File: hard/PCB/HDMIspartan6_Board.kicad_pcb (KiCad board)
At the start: 4 copper layers, 60 x 85.1 mm, 151 parts, among them IC1 W9812G6KH, J1 CONN_02X20, P1 CONN_01X03, U1 XC6SLX9-2TQG144C, U2 TPS62133RGTR, U3 ZLDO1117G33TA, U4 ZLDO1117G12TA, U5 MAX5864

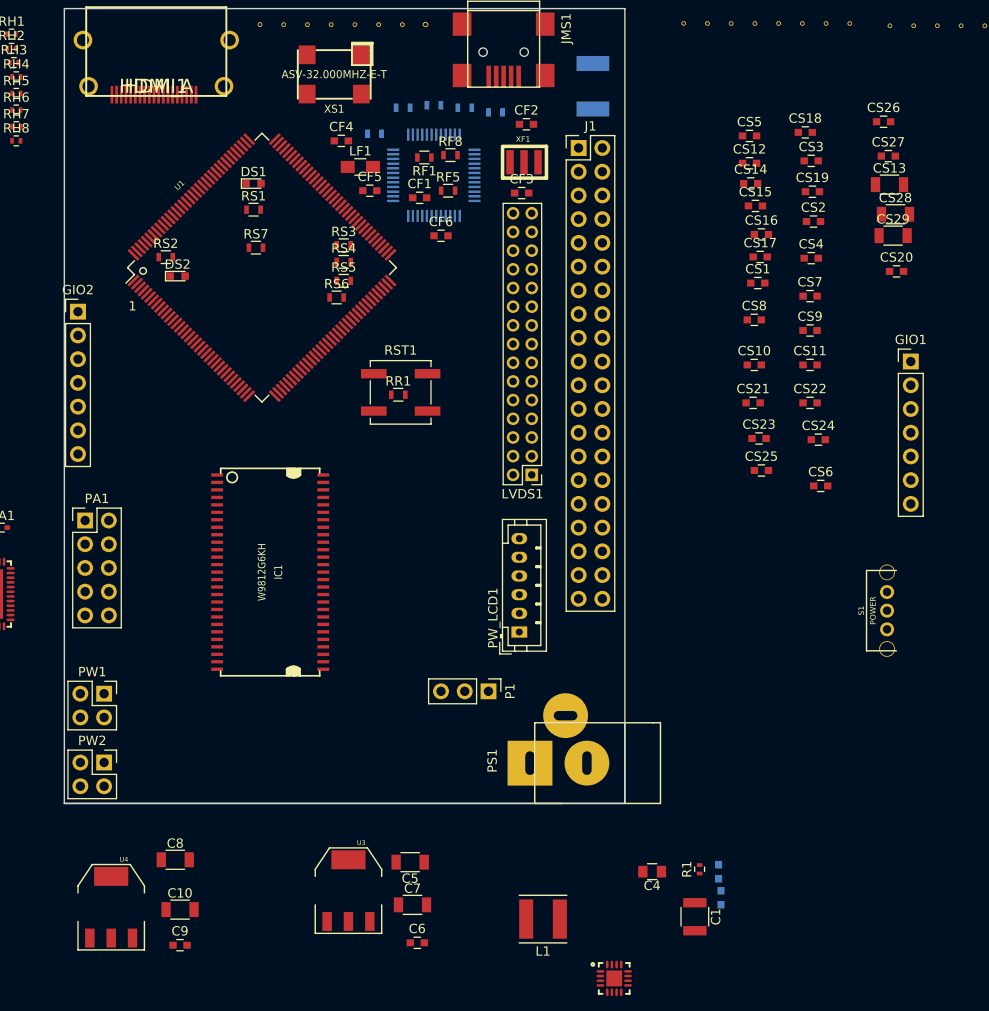
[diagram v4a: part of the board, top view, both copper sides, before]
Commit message: update 3d models
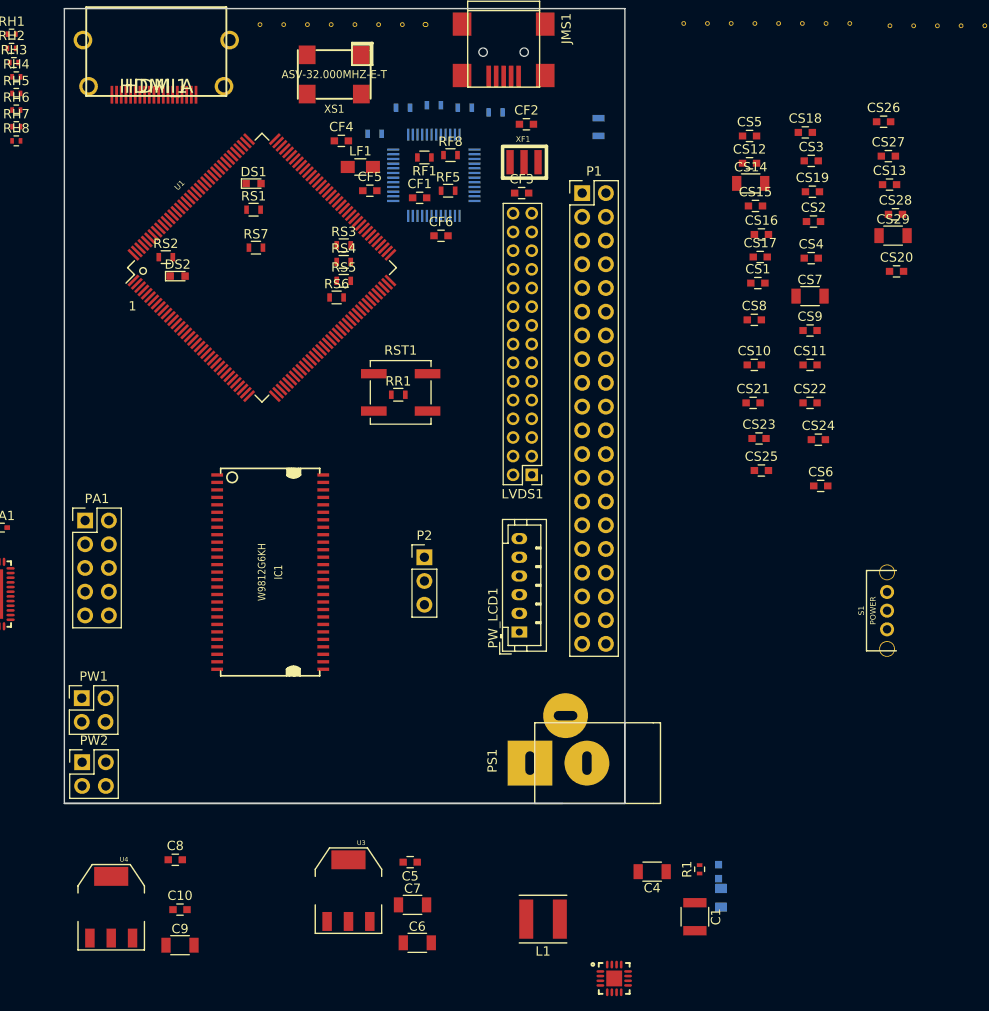
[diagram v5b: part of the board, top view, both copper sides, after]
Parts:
- removed GIO1, GIO2: CONN_01X07, Pin_Headers:Pin_Header_Straight_1x07_Pitch2.54mm
- removed J1: CONN_02X20, Pin_Headers:Pin_Header_Straight_2x20_Pitch2.54mm
- added P2: CONN_01X03, Pin_Headers:Pin_Header_Straight_1x03_Pitch2.54mm, F.Cu at (95.2, 96.3)
- C10: value 33uF -> 3.3nF; footprint Capacitors_SMD:C_1206 -> Capacitors_SMD:C_0603
- C3: value 3.3nF -> 22uF; footprint Capacitors_SMD:C_0603 -> Capacitors_SMD:C_0805
- C4: value 22uF -> 33uF; footprint Capacitors_SMD:C_0805 -> Capacitors_SMD:C_1206
- C5, C8: value 33uF -> 100n; footprint Capacitors_SMD:C_1206 -> Capacitors_SMD:C_0603
- C6, C9: value 100n -> 33uF; footprint Capacitors_SMD:C_0603 -> Capacitors_SMD:C_1206
- CF1: value 47pF -> 10nF
- CF2: value 47pF -> 10uF
- CF3: value 10nF -> 100nF
- CF4: value 10uF -> 33nF
- CF5: value 33nF -> 47pF
- CF6: value 100nF -> 47pF
- CS11, CS26, CS27: value 1uF -> 0.1uF
- CS13, CS28: value 4.7uF -> 1uF; footprint Capacitors_SMD:C_1206 -> Capacitors_SMD:C_0603
- CS14, CS7: value 0.1uF -> 4.7uF; footprint Capacitors_SMD:C_0603 -> Capacitors_SMD:C_1206
- CS6: value 0.1uF -> 1uF
- F1: footprint Resistors_SMD:R_1812 -> Resistors_SMD:R_0805
- P1: value CONN_01X03 -> CONN_02X20; footprint Socket_Strips:Socket_Strip_Straight_1x03_Pitch2.54mm -> Pin_Headers:Pin_Header_Straight_2x20_Pitch2.54mm
- PW1, PW2: footprint Socket_Strips:Socket_Strip_Straight_2x02_Pitch2.54mm -> Pin_Headers:Pin_Header_Straight_2x02_Pitch2.54mm
- RF1: value 27R -> 470R
- RF3: value 1K5 -> 27R
- RF4: value 10K -> 15K
- RF5: value 470R -> 1K5
- RF7: value 10k -> 10K
- RF8: value 15K -> 10k
- RS1, RS2: value 1k -> 68
- RS5: value 68 -> 4.7k
- RS6: value 68 -> 1k
- RS7: value 4.7k -> 1k
- moved P1 54.3 mm to (112.1, 57.3), turned to 0 degrees
- moved F1 4.41 mm to (113.9, 50.2)
- moved PW1 2.44 mm to (58.6, 111.4)
- moved PW2 2.35 mm to (58.6, 118.2)
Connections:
- C10 pad 1: +1V2 -> Net-(C10-Pad1)
- C3 pad 1: Net-(C3-Pad1) -> VDD5V
- C4 pad 1: VDD5V -> +5V
- C5 pad 1: +5V -> +3V3
- C8 pad 1: +3V3 -> +1V2
- CA1 pad 1: /ADC_DAC/REFP -> /ADC_DAC/COM
- CA2 pad 1: /ADC_DAC/COM -> /ADC_DAC/REFN
- CA3 pad 1: /ADC_DAC/REFN -> /ADC_DAC/REFP
- CF1 pad 1: GND -> /Power/USBVCC
- CF1 pad 2: Net-(CF1-Pad2) -> GND
- CF2 pad 1: GND -> /serial_interface/+5VA
- CF2 pad 2: Net-(CF2-Pad2) -> GND
- CF3 pad 1: /Power/USBVCC -> Net-(CF3-Pad1)
- CF4 pad 1: /serial_interface/+5VA -> Net-(CF4-Pad1)
- CF5 pad 1: Net-(CF5-Pad1) -> GND
- CF5 pad 2: GND -> Net-(CF5-Pad2)
- CF6 pad 1: Net-(CF6-Pad1) -> GND
- CF6 pad 2: GND -> Net-(CF6-Pad2)
- CS10 pad 1: +3V3 -> +1V2
- CS11 pad 1: +3V3 -> +1V2
- CS12 pad 1: +3V3 -> +1V2
- CS13 pad 1: +3V3 -> +1V2
- CS14 pad 1: +3V3 -> +1V2
- CS17 pad 1: +1V2 -> +3V3
- CS19 pad 1: +1V2 -> +3V3
- CS21 pad 1: +1V2 -> +3V3
- CS23 pad 1: +1V2 -> +3V3
- CS25 pad 1: +1V2 -> +3V3
- CS27 pad 1: +1V2 -> +3V3
- CS29 pad 1: +1V2 -> +3V3
- CS8 pad 1: +3V3 -> +1V2
- CS9 pad 1: +3V3 -> +1V2
- FT1 pad 43: Net-(CF1-Pad2) -> Net-(CF5-Pad2)
- FT1 pad 44: Net-(CF2-Pad2) -> Net-(CF6-Pad2)
- FT1 pad 46: Net-(CF6-Pad1) -> Net-(CF3-Pad1)
- FT1 pad 6: Net-(CF5-Pad1) -> Net-(CF4-Pad1)
- P1 pad 1: VDD5V -> +3V3
- P1 pad 2: +5V -> VDD5V
- P1 pad 3: /Power/USBVCC -> /spartan6/SDA
- RF1 pad 1: Net-(JMS1-Pad2) -> Net-(CF3-Pad1)
- RF1 pad 2: Net-(FT1-Pad8) -> /serial_interface/+5VA
- RF2 pad 1: Net-(JMS1-Pad3) -> Net-(JMS1-Pad2)
- RF2 pad 2: Net-(FT1-Pad7) -> Net-(FT1-Pad8)
- RF3 pad 1: Net-(FT1-Pad7) -> Net-(JMS1-Pad3)
- RF3 pad 2: Net-(FT1-Pad5) -> Net-(FT1-Pad7)
- RF4 pad 1: /serial_interface/+5VA -> +3V3
- RF4 pad 2: Net-(FT1-Pad2) -> /spartan6/F_RXD
- RF5 pad 1: Net-(CF6-Pad1) -> Net-(FT1-Pad7)
- RF5 pad 2: /serial_interface/+5VA -> Net-(FT1-Pad5)
- RF7 pad 1: Net-(FT1-Pad26) -> /serial_interface/+5VA
- RF7 pad 2: +3V3 -> Net-(FT1-Pad2)
- RF8 pad 1: +3V3 -> Net-(FT1-Pad26)
- RF8 pad 2: /spartan6/F_RXD -> +3V3
- RS1 pad 1: GND -> /spartan6/F_TCK
- RS1 pad 2: Net-(DS1-Pad2) -> Net-(RS1-Pad2)
- RS2 pad 1: GND -> /spartan6/F_TDI
- RS2 pad 2: Net-(DS2-Pad2) -> Net-(RS2-Pad2)
- RS3 pad 1: /spartan6/F_TCK -> /spartan6/F_TDO
- RS4 pad 1: /spartan6/F_TDI -> /spartan6/F_TMS
- RS5 pad 1: /spartan6/F_TDO -> +3V3
- RS6 pad 1: /spartan6/F_TMS -> GND
- RS6 pad 2: Net-(RS6-Pad2) -> Net-(DS1-Pad2)
- RS7 pad 1: +3V3 -> GND
- RS7 pad 2: Net-(RS7-Pad2) -> Net-(DS2-Pad2)
- U1 pad 106: Net-(RS5-Pad2) -> Net-(RS3-Pad2)
- U1 pad 107: Net-(RS6-Pad2) -> Net-(RS4-Pad2)
- U1 pad 109: Net-(RS3-Pad2) -> Net-(RS1-Pad2)
- U1 pad 110: Net-(RS4-Pad2) -> Net-(RS2-Pad2)
- U1 pad 38: Net-(RS7-Pad2) -> Net-(RS5-Pad2)
- U2 pad 9: Net-(C3-Pad1) -> Net-(C10-Pad1)
- XF1 pad 1: Net-(CF1-Pad2) -> Net-(CF5-Pad2)
- XF1 pad 3: Net-(CF2-Pad2) -> Net-(CF6-Pad2)

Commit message: reorganización
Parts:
- LF1: footprint Resistors_SMD:R_0805_HandSoldering -> Resistors_SMD:R_0805
- moved PS1 93.5 mm to (109.7, 24.9)
- moved JMS1 75.6 mm to (38.5, 79.5)
- moved PW_LCD1 27.7 mm to (104.7, 76.6)
- moved LVDS1 25.4 mm to (105.8, 112.9)
- moved P1 21.1 mm to (123.3, 75.2)
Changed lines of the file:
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@@
-(kicad_pcb (version 4) (host pcbnew 4.0.6-e0-6349~53~ubuntu16.04.1)
+(kicad_pcb (version 4) (host pcbnew 4.0.5)
   (general
     (links 443)
@@
   )
   (module Connectors_JST:JST_PH_B6B-PH-K_06x2.00mm_Straight (layer F.Cu)
-    (at 105.4 104.286 90)
+    (at 104.71166 76.55682 90)
     (descr "JST PH series connector, B6B-PH-K, top entry type, through hole, Datasheet: http://www.jst-mfg.com/product/pdf/eng/ePH.pdf")
     (tags "connector jst ph")
@@
   )
   (module Pin_Headers:Pin_Header_Straight_2x15_Pitch2.00mm (layer F.Cu)
-    (at 106.7335 87.4585 180)
+    (at 105.82926 112.87882 180)
     (descr "Through hole straight pin header, 2x15, 2.00mm pitch, double rows")
     (tags "Through hole pin header THT 2x15 2.00mm double row")
@@
     (pad "" thru_hole circle (at 4.1 0 90) (size 1.7 1.7) (drill 1.5) (layers *.Cu *.Mask F.SilkS))
     (pad "" thru_hole circle (at -4.1 0 90) (size 1.7 1.7) (drill 1.5) (layers *.Cu *.Mask F.SilkS))
-    (model /media/raparram/E4AA707DAA704DD4/Users/Ryu/Documents/GitHub/hdmi-fpga/hard/PCB/packages3d/slide-sw-spdt-right-angle.wrl
+    (model ${KIPRJMOD}/packages3d/slide-sw-spdt-right-angle.wrl
       (at (xyz 0 0 0))
       (scale (xyz 1 1 1))
@@
   )
   (module Project:USB_Mini-B (layer F.Cu)
-    (at 103.7236 41.3575 270)
+    (at 38.45576 79.45242 270)
     (descr "USB Mini-B 5-pin SMD connector")
     (tags "USB USB_B USB_Mini connector")
@@
     (pad "" np_thru_hole circle (at 0.8509 2.19964 270) (size 0.89916 0.89916) (drill 0.89916) (layers *.Cu *.Mask F.SilkS))
     (model ${KIPRJMOD}/packages3d/usb.wrl
-      (at (xyz 0 0 0))
-      (scale (xyz 1 1 1))
-      (rotate (xyz 0 0 0))
+      (at (xyz 0.15 0 0))
+      (scale (xyz 0.42 0.42 0.42))
+      (rotate (xyz -90 0 90))
     )
   )
@@
   )
   (module Project:JACK_ALIM (layer F.Cu)
-    (at 112.639 118.3195 180)
+    (at 109.72816 24.89322 180)
     (descr "module 1 pin (ou trou mecanique de percage)")
     (tags "CONN JACK")
@@
     )
   )
-  (module Resistors_SMD:R_0805_HandSoldering (layer F.Cu)
-    (at 88.382 54.502)
-    (descr "Resistor SMD 0805, hand soldering")
-    (tags "resistor 0805")
-    (attr smd)
-    (fp_text reference LF1 (at 0 -1.7) (layer F.SilkS)
-      (effects (font (size 1 1) (thickness 0.15)))
-    )
-    (fp_text value HZ0805D152R-10 (at 0 1.75) (layer F.Fab)
-      (effects (font (size 1 1) (thickness 0.15)))
-    )
-    (fp_text user %R (at 0 0) (layer F.Fab)
-      (effects (font (size 0.5 0.5) (thickness 0.075)))
-    )
-    (fp_line (start -1 0.62) (end -1 -0.62) (layer F.Fab) (width 0.1))
-    (fp_line (start 1 0.62) (end -1 0.62) (layer F.Fab) (width 0.1))
-    (fp_line (start 1 -0.62) (end 1 0.62) (layer F.Fab) (width 0.1))
-    (fp_line (start -1 -0.62) (end 1 -0.62) (layer F.Fab) (width 0.1))
-    (fp_line (start 0.6 0.88) (end -0.6 0.88) (layer F.SilkS) (width 0.12))
-    (fp_line (start -0.6 -0.88) (end 0.6 -0.88) (layer F.SilkS) (width 0.12))
-    (fp_line (start -2.35 -0.9) (end 2.35 -0.9) (layer F.CrtYd) (width 0.05))
-    (fp_line (start -2.35 -0.9) (end -2.35 0.9) (layer F.CrtYd) (width 0.05))
-    (fp_line (start 2.35 0.9) (end 2.35 -0.9) (layer F.CrtYd) (width 0.05))
-    (fp_line (start 2.35 0.9) (end -2.35 0.9) (layer F.CrtYd) (width 0.05))
-    (pad 1 smd rect (at -1.35 0) (size 1.5 1.3) (layers F.Cu F.Paste F.Mask)
-      (net 51 /Power/USBVCC))
-    (pad 2 smd rect (at 1.35 0) (size 1.5 1.3) (layers F.Cu F.Paste F.Mask)
-      (net 80 /serial_interface/+5VA))
-    (model ${KISYS3DMOD}/Resistors_SMD.3dshapes/R_0805.wrl
-      (at (xyz 0 0 0))
-      (scale (xyz 1 1 1))
-      (rotate (xyz 0 0 0))
-    )
-  )
   (module Resistors_SMD:R_0402 (layer F.Cu)
     (at 51.044 40.278)
@@
     (model ${KIPRJMOD}/packages3d/Crystal_SMD_5032-4pin_5.0x3.2mm.wrl
       (at (xyz 0 0 0))
-      (scale (xyz 1 1 1))
+      (scale (xyz 1.55 1.55 1.55))
       (rotate (xyz 0 0 0))
     )
@@
   )
   (module Pin_Headers:Pin_Header_Straight_2x20_Pitch2.54mm (layer F.Cu)
-    (at 112.131 57.296)
+    (at 123.34256 75.18522)
     (descr "Through hole straight pin header, 2x20, 2.54mm pitch, double rows")
     (tags "Through hole pin header THT 2x20 2.54mm double row")
@@
     )
   )
+  (module Resistors_SMD:R_0805 (layer F.Cu)
+    (at 88.382 54.502)
+    (descr "Resistor SMD 0805, reflow soldering, Vishay (see dcrcw.pdf)")
+    (tags "resistor 0805")
+    (attr smd)
+    (fp_text reference LF1 (at 0 -1.65) (layer F.SilkS)
+      (effects (font (size 1 1) (thickness 0.15)))
+    )
+    (fp_text value HZ0805D152R-10 (at 0 1.75) (layer F.Fab)
+      (effects (font (size 1 1) (thickness 0.15)))
+    )
+    (fp_text user %R (at 0 0) (layer F.Fab)
+      (effects (font (size 0.5 0.5) (thickness 0.075)))
+    )
+    (fp_line (start -1 0.62) (end -1 -0.62) (layer F.Fab) (width 0.1))
+    (fp_line (start 1 0.62) (end -1 0.62) (layer F.Fab) (width 0.1))
+    (fp_line (start 1 -0.62) (end 1 0.62) (layer F.Fab) (width 0.1))
+    (fp_line (start -1 -0.62) (end 1 -0.62) (layer F.Fab) (width 0.1))
+    (fp_line (start 0.6 0.88) (end -0.6 0.88) (layer F.SilkS) (width 0.12))
+    (fp_line (start -0.6 -0.88) (end 0.6 -0.88) (layer F.SilkS) (width 0.12))
+    (fp_line (start -1.55 -0.9) (end 1.55 -0.9) (layer F.CrtYd) (width 0.05))
+    (fp_line (start -1.55 -0.9) (end -1.55 0.9) (layer F.CrtYd) (width 0.05))
+    (fp_line (start 1.55 0.9) (end 1.55 -0.9) (layer F.CrtYd) (width 0.05))
+    (fp_line (start 1.55 0.9) (end -1.55 0.9) (layer F.CrtYd) (width 0.05))
+    (pad 1 smd rect (at -0.95 0) (size 0.7 1.3) (layers F.Cu F.Paste F.Mask)
+      (net 51 /Power/USBVCC))
+    (pad 2 smd rect (at 0.95 0) (size 0.7 1.3) (layers F.Cu F.Paste F.Mask)
+      (net 80 /serial_interface/+5VA))
+    (model ${KISYS3DMOD}/Resistors_SMD.3dshapes/R_0805.wrl
+      (at (xyz 0 0 0))
+      (scale (xyz 1 1 1))
+      (rotate (xyz 0 0 0))
+    )
+  )

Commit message: update layout
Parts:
- removed PW1, PW2: CONN_02X02, Pin_Headers:Pin_Header_Straight_2x02_Pitch2.54mm
- removed TH21, TH27, TH33, TH39: CONN_1, Project:1Pin_12mil_VIA
- added ?: , Project:RPi_Hat_Mounting_Hole, F.Cu at (160.9, 63.2)
- added ?: , Project:RPi_Hat_Mounting_Hole, F.Cu at (111.8, 121.2)
- added ?: , Project:RPi_Hat_Mounting_Hole, F.Cu at (111.8, 63.2)
- added TH51, TH52, TH53, TH54: CONN_1, Project:1Pin_12mil_VIA, F.Cu at (37.6, 142.1)
- C2, C3, RF4, RF6, RF7: moved to F.Cu
- C4, C5, C6, C7, C8, C9, CA1, CA2, CA3, IC1, RR1: moved to B.Cu
- LF1: footprint Resistors_SMD:R_0805 -> Resistors_SMD:R_0805_HandSoldering
- LVDS1: value CONN_02X15 -> CONN_02X09; footprint Pin_Headers:Pin_Header_Straight_2x15_Pitch2.00mm -> Project:LVDS_SMD
- P2: footprint Pin_Headers:Pin_Header_Straight_1x03_Pitch2.54mm -> Socket_Strips:Socket_Strip_Straight_1x03_Pitch2.54mm
- moved TH35 252.7 mm to (-2.68, 143.1), turned to 270 degrees
- moved TH36 248.1 mm to (-0.14, 143.1), turned to 270 degrees
- moved TH32 243.5 mm to (2.40, 143.1), turned to 270 degrees
- moved TH37 238.9 mm to (4.94, 143.1), turned to 270 degrees
- moved TH31 234.3 mm to (7.48, 143.1), turned to 270 degrees
- moved TH48 222.6 mm to (13.9, 142.7), turned to 270 degrees
- moved TH49 220.7 mm to (15.1, 143.0), turned to 270 degrees
- moved TH46 218.1 mm to (16.6, 143.1), turned to 270 degrees
- moved TH45 215.8 mm to (17.9, 143.1), turned to 270 degrees
- moved TH44 212.8 mm to (19.6, 143.1), turned to 270 degrees
- moved TH50 211.0 mm to (20.1, 142.0), turned to 180 degrees
- moved TH15 203.7 mm to (24.8, 142.9), turned to 180 degrees
- moved TH12 199.3 mm to (27.4, 142.9), turned to 180 degrees
- moved TH1 195.0 mm to (29.9, 142.9), turned to 180 degrees
- moved TH34 187.7 mm to (34.2, 142.9), turned to 180 degrees
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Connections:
- S1 pad 1: VCC -> Net-(S1-Pad1)
- S1 pad 3: Net-(S1-Pad3) -> VCC
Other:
- board size 60 x 85.1 mm -> 56.1 x 89.6 mm
- board text added: "2"
- board text removed: "1"

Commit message: Test LVDS RAM
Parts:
- moved P1 0.10 mm to (111.9, 66.7)
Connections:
- P1 pad 1: +3V3 -> Net-(P1-Pad1)
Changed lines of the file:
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@@
 (kicad_pcb (version 4) (host pcbnew 4.0.6-e0-6349~53~ubuntu16.04.1)
   (general
-    (links 435)
-    (no_connects 413)
+    (links 434)
+    (no_connects 412)
     (area 108.230759 59.595899 164.453801 149.311381)
     (thickness 1.6)
@@
     (zones 0)
     (modules 150)
-    (nets 234)
+    (nets 235)
   )
   (page A4)
@@
   (net 232 "Net-(RS2-Pad2)")
   (net 233 "Net-(S1-Pad1)")
+  (net 234 "Net-(P1-Pad1)")
   (net_class Default "This is the default net class."
     (clearance 0.15)
@@
     (add_net "Net-(JMS1-Pad4)")
     (add_net "Net-(L1-Pad2)")
+    (add_net "Net-(P1-Pad1)")
     (add_net "Net-(P1-Pad11)")
     (add_net "Net-(P1-Pad12)")
@@
   )
   (module Pin_Headers:Pin_Header_Straight_2x20_Pitch2.54mm locked (layer F.Cu)
-    (at 111.83128 66.69908 180)
+    (at 111.9278 66.694 180)
     (descr "Through hole straight pin header, 2x20, 2.54mm pitch, double rows")
     (tags "Through hole pin header THT 2x20 2.54mm double row")
@@
     )
     (pad 1 thru_hole rect (at -1.19126 -49.59858 180) (size 1.7 1.7) (drill 1) (layers *.Cu *.Mask)
-      (net 13 +3V3))
+      (net 234 "Net-(P1-Pad1)"))
     (pad 2 thru_hole oval (at 1.34874 -49.59858 180) (size 1.7 1.7) (drill 1) (layers *.Cu *.Mask)
       (net 50 VDD5V))
